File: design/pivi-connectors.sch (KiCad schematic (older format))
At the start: 13 parts, among them P1 Recom_Power_RAC10-05SC/277, P3 CONN_01X05, P4 CONN_01X02, P6 CONN_01X02, P7 CONN_01X05, P8 CONN_01X02, P9 CONN_02X20

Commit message: Fix #4: add GPIO to reset microcontroller from pi.
* Add a Raspeberry pi pin (GPIO 18) to reset microcontroller.
* Add a Raspebeery pi pin (GPIO 23) to control the microcontroller status.
* Add a RGB LED connected to the microcontroller (PD0, PD1, PD2).
* Rename all the sheets to PIVI v1.1.
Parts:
- C21: symbol C -> C-RESCUE-pivi-shield
- R9: symbol R -> R-RESCUE-pivi-shield
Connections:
- net labels added: GPIO-18, GPIO-23
- wire segments 48 -> 50
- no-connect marks 26 -> 24
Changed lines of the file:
@@
 EESchema Schematic File Version 2
+LIBS:pivi-shield-rescue
 LIBS:power
 LIBS:device
@@
 LIBS:memory
 LIBS:xilinx
-LIBS:special
 LIBS:microcontrollers
 LIBS:dsp
@@
 LIBS:txs0104e
 LIBS:less
+LIBS:pivi-shield-cache
 EELAYER 25 0
 EELAYER END
@@
 Sheet 3 12
 Title "PIVI"
-Date "sáb 01 nov 2014"
-Rev "1.0"
+Date "mar 23 jun 2015"
+Rev "1.1"
 Comp "Copyright (C) LESS industries S.A. 2014,2015"
 Comment1 "Share alike attribution non-commercial 4.0"
@@
 $EndDescr
 $Comp
-L +5V #PWR025
+L +5V #PWR026
 U 1 1 54959F0D
 P 7425 1625
-F 0 "#PWR025" H 7425 1715 20  0001 C CNN
+F 0 "#PWR026" H 7425 1715 20  0001 C CNN
 F 1 "+5V" H 7425 1750 30  0000 C CNN
 F 2 "" H 7425 1625 60  0000 C CNN
@@
 $EndComp
 $Comp
-L C C21
+L C-RESCUE-pivi-shield C21
 U 1 1 54959F13
 P 7425 1850
+AR Path="/54959F13" Ref="C21"  Part="1"
+AR Path="/549598FF/54959F13" Ref="C21"  Part="1"
 F 0 "C21" H 7425 1950 40  0000 L CNN
 F 1 "100nF" H 7431 1765 40  0000 L CNN
@@
 NoConn ~ 6550 2650
 NoConn ~ 6550 2450
-NoConn ~ 6550 2350
-NoConn ~ 6550 2150
 NoConn ~ 6550 3550
 NoConn ~ 6550 3450
@@
 Power line output.\nTo load.
 $Comp
-L +5V #PWR026
+L +5V #PWR027
 U 1 1 54959F4A
 P 3000 4675
-F 0 "#PWR026" H 3000 4765 20  0001 C CNN
+F 0 "#PWR027" H 3000 4765 20  0001 C CNN
 F 1 "+5V" H 3000 4800 30  0000 C CNN
 F 2 "" H 3000 4675 60  0000 C CNN
@@
 Power Line Connections
 $Comp
-L R R9
+L R-RESCUE-pivi-shield R9
 U 1 1 54959F58
 P 4425 4975
@@
 	1300 4575 1400 4575
 $Comp
-L GND #PWR027
+L GND-RESCUE-pivi-shield #PWR028
 U 1 1 54BFA08A
 P 7425 2075
-F 0 "#PWR027" H 7425 1825 60  0001 C CNN
+F 0 "#PWR028" H 7425 1825 60  0001 C CNN
 F 1 "GND" H 7425 1925 60  0000 C CNN
 F 2 "" H 7425 2075 60  0000 C CNN
@@
 $EndComp
 $Comp
-L GND #PWR028
+L GND-RESCUE-pivi-shield #PWR029
 U 1 1 54BFA09E
 P 6725 3300
-F 0 "#PWR028" H 6725 3050 60  0001 C CNN
+F 0 "#PWR029" H 6725 3050 60  0001 C CNN
 F 1 "GND" H 6725 3150 60  0000 C CNN
 F 2 "" H 6725 3300 60  0000 C CNN
@@
 $EndComp
 $Comp
-L GND #PWR029
+L GND-RESCUE-pivi-shield #PWR030
 U 1 1 54BFA0B2
 P 5900 3700
-F 0 "#PWR029" H 5900 3450 60  0001 C CNN
+F 0 "#PWR030" H 5900 3450 60  0001 C CNN
 F 1 "GND" H 5900 3550 60  0000 C CNN
 F 2 "" H 5900 3700 60  0000 C CNN
@@
 $EndComp
 $Comp
-L GND #PWR030
+L GND-RESCUE-pivi-shield #PWR031
 U 1 1 54BFA0C6
 P 4425 5275
-F 0 "#PWR030" H 4425 5025 60  0001 C CNN
+F 0 "#PWR031" H 4425 5025 60  0001 C CNN
 F 1 "GND" H 4425 5125 60  0000 C CNN
 F 2 "" H 4425 5275 60  0000 C CNN
@@
 $EndComp
 $Comp
-L GND #PWR031
+L GND-RESCUE-pivi-shield #PWR032
 U 1 1 54BFA203
 P 2625 4675
-F 0 "#PWR031" H 2625 4425 60  0001 C CNN
+F 0 "#PWR032" H 2625 4425 60  0001 C CNN
 F 1 "GND" H 2625 4525 60  0000 C CNN
 F 2 "" H 2625 4675 60  0000 C CNN
@@
 Alternative 5V power supply \nfor using when powering \nthe board externally.
 $Comp
-L GND #PWR032
+L GND-RESCUE-pivi-shield #PWR033
 U 1 1 54C181FB
 P 1350 5625
-F 0 "#PWR032" H 1350 5375 60  0001 C CNN
+F 0 "#PWR033" H 1350 5375 60  0001 C CNN
 F 1 "GND" H 1350 5475 60  0000 C CNN
 F 2 "" H 1350 5625 60  0000 C CNN
@@
 	1    0    0    -1
 $EndComp
+Wire Wire Line
+	6550 2150 6875 2150
+Text HLabel 6875 2150 2    60   Input ~ 0
+GPIO-18
+Wire Wire Line
+	6550 2350 6875 2350
+Text HLabel 6875 2350 2    60   Input ~ 0
+GPIO-23
 $EndSCHEMATC

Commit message: Fix #4: Move RGB LED from microcontroller to pi.
* Move RGB LED. Now it is controlled by the raspberry pi.
* Change some new libraries for capacitors and resistors.
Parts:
- added D2: LED_RGB, symbol LED_RGB
- added R1, R2, R3: 270, symbol R
- C21: symbol C-RESCUE-pivi-shield -> C
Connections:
- net labels added: GPIO-12, GPIO-24, GPIO-25
- wire segments 50 -> 64
- no-connect marks 24 -> 21
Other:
- note added: "The GPIO pins can draw 50mA safely, distributed\nacross all the pins; an individual GPIO pin can \nonly safely draw 16mA. \n\nhttps://www.raspberrypi.org/documentation/hardware/\nraspberrypi/power/README.md"
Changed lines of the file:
@@
 LIBS:txs0104e
 LIBS:less
-LIBS:pivi-shield-cache
 EELAYER 25 0
 EELAYER END
@@
 $EndDescr
 $Comp
-L +5V #PWR026
+L +5V #PWR025
 U 1 1 54959F0D
 P 7425 1625
-F 0 "#PWR026" H 7425 1715 20  0001 C CNN
+F 0 "#PWR025" H 7425 1715 20  0001 C CNN
 F 1 "+5V" H 7425 1750 30  0000 C CNN
 F 2 "" H 7425 1625 60  0000 C CNN
@@
 $EndComp
 $Comp
-L C-RESCUE-pivi-shield C21
+L C C21
 U 1 1 54959F13
 P 7425 1850
@@
 NoConn ~ 6550 2850
 NoConn ~ 6550 2750
-NoConn ~ 6550 2650
-NoConn ~ 6550 2450
 NoConn ~ 6550 3550
 NoConn ~ 6550 3450
 NoConn ~ 6550 3350
-NoConn ~ 6550 3150
 NoConn ~ 6050 3450
 NoConn ~ 6050 3350
@@
 Power line output.\nTo load.
 $Comp
-L +5V #PWR027
+L +5V #PWR026
 U 1 1 54959F4A
 P 3000 4675
-F 0 "#PWR027" H 3000 4765 20  0001 C CNN
+F 0 "#PWR026" H 3000 4765 20  0001 C CNN
 F 1 "+5V" H 3000 4800 30  0000 C CNN
 F 2 "" H 3000 4675 60  0000 C CNN
@@
 	6625 1750 6625 1650
 Wire Wire Line
-	7425 2050 7425 2075
-Wire Wire Line
-	7425 1650 7425 1625
+	7425 2000 7425 2075
+Wire Wire Line
+	7425 1625 7425 1700
 Wire Wire Line
 	6550 1850 6725 1850
@@
 	1300 4575 1400 4575
 $Comp
-L GND-RESCUE-pivi-shield #PWR028
+L GND-RESCUE-pivi-shield #PWR027
 U 1 1 54BFA08A
 P 7425 2075
-F 0 "#PWR028" H 7425 1825 60  0001 C CNN
+F 0 "#PWR027" H 7425 1825 60  0001 C CNN
 F 1 "GND" H 7425 1925 60  0000 C CNN
 F 2 "" H 7425 2075 60  0000 C CNN
@@
 $EndComp
 $Comp
-L GND-RESCUE-pivi-shield #PWR029
+L GND-RESCUE-pivi-shield #PWR028
 U 1 1 54BFA09E
 P 6725 3300
-F 0 "#PWR029" H 6725 3050 60  0001 C CNN
+F 0 "#PWR028" H 6725 3050 60  0001 C CNN
 F 1 "GND" H 6725 3150 60  0000 C CNN
 F 2 "" H 6725 3300 60  0000 C CNN
@@
 $EndComp
 $Comp
-L GND-RESCUE-pivi-shield #PWR030
+L GND-RESCUE-pivi-shield #PWR029
 U 1 1 54BFA0B2
 P 5900 3700
-F 0 "#PWR030" H 5900 3450 60  0001 C CNN
+F 0 "#PWR029" H 5900 3450 60  0001 C CNN
 F 1 "GND" H 5900 3550 60  0000 C CNN
 F 2 "" H 5900 3700 60  0000 C CNN
@@
 $EndComp
 $Comp
-L GND-RESCUE-pivi-shield #PWR031
+L GND-RESCUE-pivi-shield #PWR030
 U 1 1 54BFA0C6
 P 4425 5275
-F 0 "#PWR031" H 4425 5025 60  0001 C CNN
+F 0 "#PWR030" H 4425 5025 60  0001 C CNN
 F 1 "GND" H 4425 5125 60  0000 C CNN
 F 2 "" H 4425 5275 60  0000 C CNN
@@
 $EndComp
 $Comp
-L GND-RESCUE-pivi-shield #PWR032
+L GND-RESCUE-pivi-shield #PWR031
 U 1 1 54BFA203
 P 2625 4675
-F 0 "#PWR032" H 2625 4425 60  0001 C CNN
+F 0 "#PWR031" H 2625 4425 60  0001 C CNN
 F 1 "GND" H 2625 4525 60  0000 C CNN
 F 2 "" H 2625 4675 60  0000 C CNN
@@
 Alternative 5V power supply \nfor using when powering \nthe board externally.
 $Comp
-L GND-RESCUE-pivi-shield #PWR033
+L GND-RESCUE-pivi-shield #PWR032
 U 1 1 54C181FB
 P 1350 5625
-F 0 "#PWR033" H 1350 5375 60  0001 C CNN
+F 0 "#PWR032" H 1350 5375 60  0001 C CNN
 F 1 "GND" H 1350 5475 60  0000 C CNN
 F 2 "" H 1350 5625 60  0000 C CNN
@@
 Text HLabel 6875 2350 2    60   Input ~ 0
 GPIO-23
+Connection ~ 7425 1650
+$Comp
+L LED_RGB D2
+U 1 1 558C1006
+P 7600 2950
+F 0 "D2" H 7600 3400 50  0000 C CNN
+F 1 "LED_RGB" H 7600 3300 50  0000 C CNN
+F 2 "" H 7600 2900 60  0000 C CNN
+F 3 "" H 7600 2900 60  0000 C CNN
+	1    7600 2950
+	-1   0    0    1
+$EndComp
+$Comp
+L R R1
+U 1 1 558C1041
+P 8175 2750
+F 0 "R1" V 8255 2750 50  0000 C CNN
+F 1 "270" V 8175 2750 50  0000 C CNN
+F 2 "" V 8105 2750 30  0000 C CNN
+F 3 "" H 8175 2750 30  0000 C CNN
+	1    8175 2750
+	0    -1   -1   0
+$EndComp
+$Comp
+L R R2
+U 1 1 558C1113
+P 8175 2950
+F 0 "R2" V 8255 2950 50  0000 C CNN
+F 1 "270" V 8175 2950 50  0000 C CNN
+F 2 "" V 8105 2950 30  0000 C CNN
+F 3 "" H 8175 2950 30  0000 C CNN
+	1    8175 2950
+	0    -1   -1   0
+$EndComp
+$Comp
+L R R3
+U 1 1 558C1151
+P 8175 3150
+F 0 "R3" V 8255 3150 50  0000 C CNN
+F 1 "270" V 8175 3150 50  0000 C CNN
+F 2 "" V 8105 3150 30  0000 C CNN
+F 3 "" H 8175 3150 30  0000 C CNN
+	1    8175 3150
+	0    -1   -1   0
+$EndComp
+Wire Wire Line
+	7900 2750 8025 2750
+Wire Wire Line
+	7900 2950 8025 2950
+Wire Wire Line
+	7900 3150 8025 3150
+Wire Wire Line
+	8325 2750 8550 2750
+Wire Wire Line
+	8550 2750 8550 3350
+Wire Wire Line
+	8325 3150 8550 3150
+Connection ~ 8550 3150
+Wire Wire Line
+	8325 2950 8550 2950
+Connection ~ 8550 2950
+Text Label 6875 2750 0    60   ~ 0
+GPIO-24
+Wire Wire Line
+	6550 2650 6800 2650
+Wire Wire Line
+	6800 2650 6800 2950
+Text Label 6875 2950 0    60   ~ 0
+GPIO-25
+Wire Wire Line
+	6875 2450 6875 2750
+Wire Wire Line
+	6875 2450 6550 2450
+Wire Wire Line
+	6550 3150 7300 3150
+Text Label 6875 3150 0    60   ~ 0
+GPIO-12
+$Comp
+L GND #PWR033
+U 1 1 558C16FC
+P 8550 3350
+F 0 "#PWR033" H 8550 3100 50  0001 C CNN
+F 1 "GND" H 8550 3200 50  0000 C CNN
+F 2 "" H 8550 3350 60  0000 C CNN
+F 3 "" H 8550 3350 60  0000 C CNN
+	1    8550 3350
+	1    0    0    -1
+$EndComp
+Text Notes 8650 3200 0    60   ~ 0
+The GPIO pins can draw 50mA safely, distributed\nacross all the pins; an individual GPIO pin can \nonly safely draw 16mA. \n\nhttps://www.raspberrypi.org/documentation/hardware/\nraspberrypi/power/README.md
+Wire Wire Line
+	6800 2950 7300 2950
+Wire Wire Line
+	6875 2750 7300 2750
 $EndSCHEMATC

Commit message: Changing footprints of  audio jack3.5mm Added new footprints. Added debub uart,  reference voltage Added two extra circuits for voltage measure Moving to PIVI 2.0, added circuits for current clamps
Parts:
- removed P3, P7: CONN_01X05, LESS:CONN-TERM-BLK-5POS-PHOENIX, symbol CONN_01X05
- removed P8: CONN_01X02, LESS:CONN-TERM-BLK-2POS-PHOENIX, symbol CONN_01X02
- removed R1, R2, R3: 270, symbol R
- added P6: CONN_01X04, symbol CONN_01X04
- added R7, R8, R9: 270, Resistors_SMD:R_0603, symbol R
- D2: footprint (none) -> LEDs:LED_RGB_PLLC-6
- R6: renamed from R9; symbol R-RESCUE-pivi-shield -> R
- renumbered C21 to C11, L15 to L4, L16 to L5, P6 to P2, P1 to P3, P9 to P5
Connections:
- net labels added: +3.3VP, CT1_1, CT1_2, CT1_DETECTOR, CT2_1, CT2_2, CT2_DETECTOR, CT3_1, CT3_2, CT3_DETECTOR, CT4_1, CT4_2, CT4_DETECTOR, CT5_1, CT5_2, CT5_DETECTOR, CT6_1, CT6_2, CT6_DETECTOR, Neutral_Line, Phase_Line
- net labels removed: Neutral1_In, Neutral1_Out, Phase1_In, Phase1_Out, Phase2_In, Phase2_Out, Phase3_In, Phase3_Out, Phase4_In, Phase4_Out, Phase5_In, Phase5_Out, Phase6_In, Phase6_Out
- wire segments 64 -> 78
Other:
- note added: "Audio Jack 3.5 mm female connector\n"
- note added: "Clamp audio connections for SCT-013-000"
- note added: "Debug Uart"
- note added: "SJ-3506-SMT"
- note added: "The GPIO pins can draw 50mA safely, distributed\nacross all the pins; an individual GPIO pin can \nonly safely draw 16mA. \n\nhttps://www.raspberrypi.org/documentation/hardw"
- note added: "This connector must meet the following requirements:\n* Internal switch : Avoids noise in pins when the clamp is unplugged.\n* Shielded : Increase endurance, stregth and avoid noise."
- note removed: "277-9761-ND"
- note removed: "Power line output.\nTo load."
- note removed: "The GPIO pins can draw 50mA safely, distributed\nacross all the pins; an individual GPIO pin can \nonly safely draw 16mA. \n\nhttps://www.raspberrypi.org/documentation/hardware/\nraspberrypi/power/README.md"
- moved on the sheet: C11, D1, JP1, L4, L5, P2, P3, P4, P5

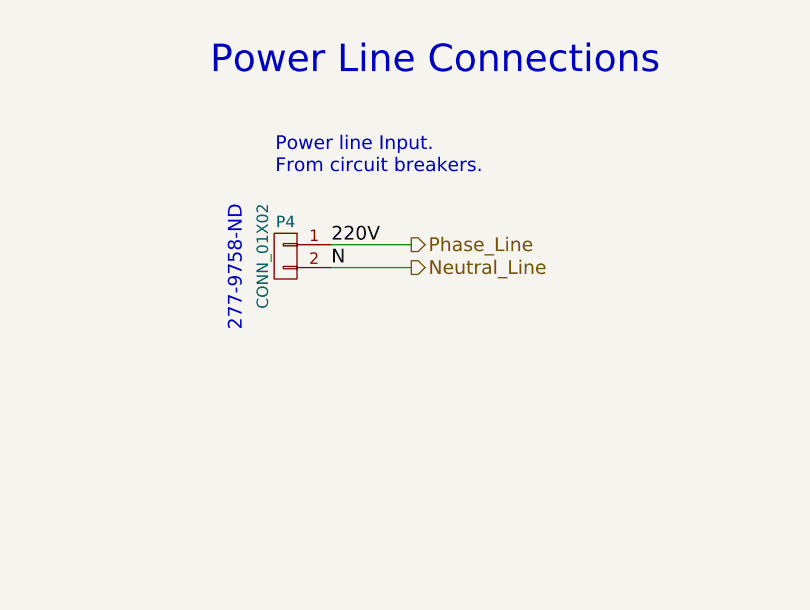
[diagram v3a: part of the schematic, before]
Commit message: Fix connection problems.
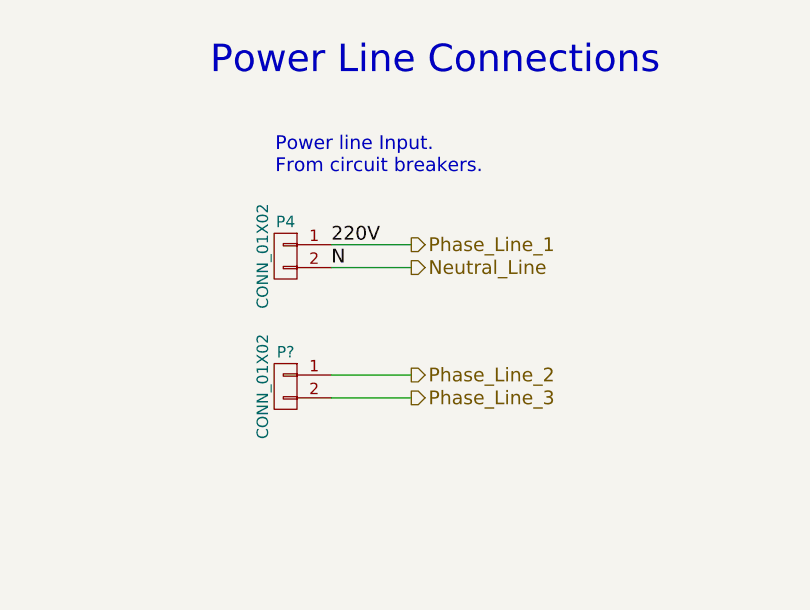
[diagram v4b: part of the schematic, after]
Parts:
- added P?: CONN_01X02, LESS:CONN-TERM-BLK-2POS-PHOENIX, symbol CONN_01X02
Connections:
- net Phase_Line renamed Phase_Line_1
- new net Phase_Line_2: P?.1 (P1)
- new net Phase_Line_3: P?.2 (P2)
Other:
- note removed: "277-9758-ND"
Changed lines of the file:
@@
 Board power Supply Connections
 Text HLabel 6610 5160 2    60   Output ~ 0
-Phase_Line
+Phase_Line_1
 Text HLabel 6610 5260 2    60   Output ~ 0
 Neutral_Line
@@
 F4 "CT_DETECTOR" I L 1450 2000 60
 $EndSheet
-Text Notes 5875 5540 1    60   ~ 0
-277-9758-ND
 Text HLabel 1300 2000 0    60   Input ~ 0
 CT1_DETECTOR
@@
 Wire Wire Line
 	9070 5205 9240 5205
+Text HLabel 6610 5730 2    60   Output ~ 0
+Phase_Line_2
+Text HLabel 6610 5830 2    60   Output ~ 0
+Phase_Line_3
+$Comp
+L CONN_01X02 P?
+U 1 1 55BC87D7
+P 6060 5780
+F 0 "P?" H 6060 5930 50  0000 C CNN
+F 1 "CONN_01X02" V 6160 5780 50  0000 C CNN
+F 2 "LESS:CONN-TERM-BLK-2POS-PHOENIX" H 6060 5780 60  0001 C CNN
+F 3 "" H 6060 5780 60  0000 C CNN
+	1    6060 5780
+	-1   0    0    -1
+$EndComp
+Wire Wire Line
+	6260 5830 6610 5830
+Wire Wire Line
+	6260 5730 6610 5730
 $EndSCHEMATC

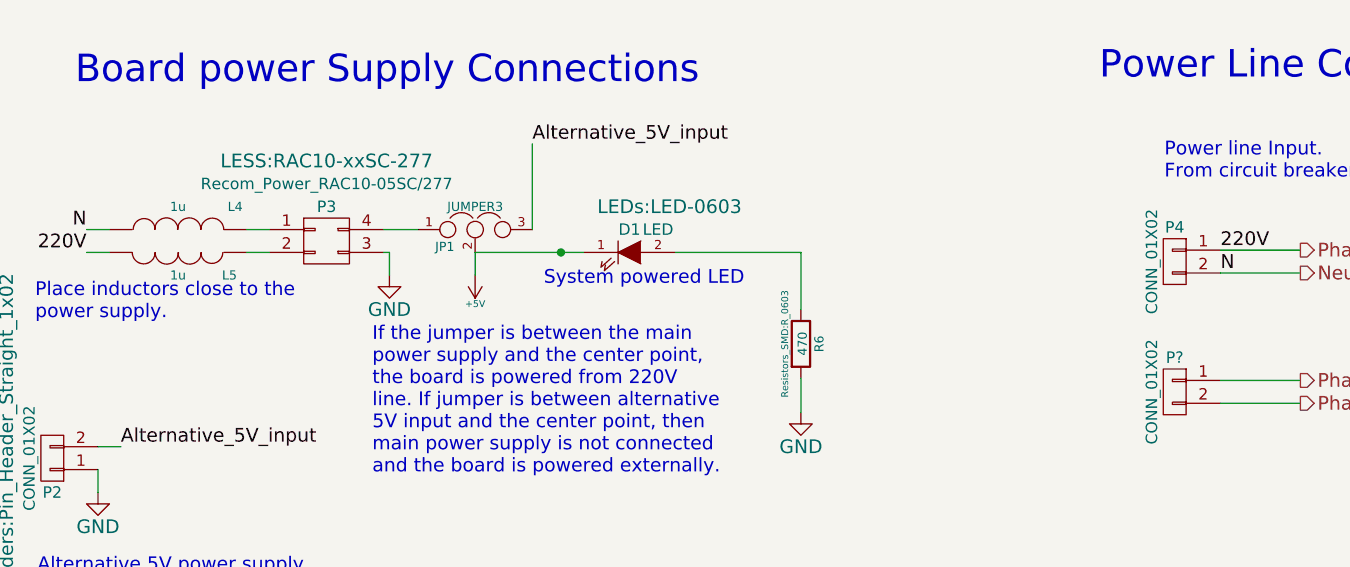
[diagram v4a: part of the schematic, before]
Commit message: Starting PIVI 2.0 * sch ready. * components in PCB placed.
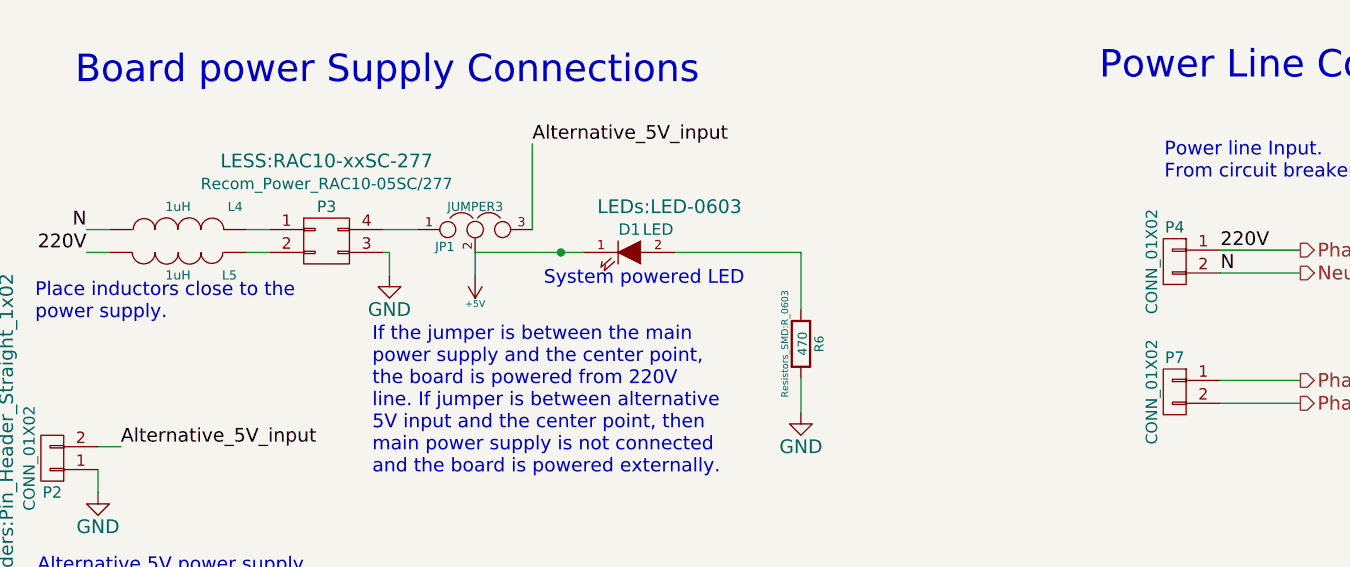
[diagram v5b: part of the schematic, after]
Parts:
- L4, L5: value 1u -> 1uH
- P4: footprint LESS:CONN-TERM-BLK-2POS-PHOENIX -> Connect:bornier2
- P6: footprint (none) -> Pin_Headers:Pin_Header_Straight_1x04
- P7: renamed from P?; footprint LESS:CONN-TERM-BLK-2POS-PHOENIX -> Connect:bornier2
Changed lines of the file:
@@
 $EndDescr
 $Comp
-L +5V #PWR27
+L +5V #PWR026
 U 1 1 54959F0D
 P 8390 1240
-F 0 "#PWR27" H 8390 1330 20  0001 C CNN
+F 0 "#PWR026" H 8390 1330 20  0001 C CNN
 F 1 "+5V" H 8390 1365 30  0000 C CNN
 F 2 "" H 8390 1240 60  0000 C CNN
@@
 Power line Input.\nFrom circuit breakers.
 $Comp
-L +5V #PWR23
+L +5V #PWR027
 U 1 1 54959F4A
 P 3000 5270
-F 0 "#PWR23" H 3000 5360 20  0001 C CNN
+F 0 "#PWR027" H 3000 5360 20  0001 C CNN
 F 1 "+5V" H 3000 5395 30  0000 C CNN
 F 2 "" H 3000 5270 60  0000 C CNN
@@
 P 1700 5070
 F 0 "L4" V 1800 4820 40  0000 C CNN
-F 1 "1u" V 1800 5070 40  0000 C CNN
+F 1 "1uH" V 1800 5070 40  0000 C CNN
 F 2 "SMD_Packages:SMD-0603" H 1700 5070 60  0001 C CNN
 F 3 "" H 1700 5070 60  0000 C CNN
@@
 P 1700 5170
 F 0 "L5" V 1800 5395 40  0000 C CNN
-F 1 "1u" V 1800 5170 40  0000 C CNN
+F 1 "1uH" V 1800 5170 40  0000 C CNN
 F 2 "SMD_Packages:SMD-0603" H 1700 5170 60  0001 C CNN
 F 3 "" H 1700 5170 60  0000 C CNN
@@
 $EndComp
 $Comp
-L GND #PWR28
+L GND #PWR028
 U 1 1 54BFA08A
 P 8390 1690
-F 0 "#PWR28" H 8390 1440 60  0001 C CNN
+F 0 "#PWR028" H 8390 1440 60  0001 C CNN
 F 1 "GND" H 8390 1540 60  0000 C CNN
 F 2 "" H 8390 1690 60  0000 C CNN
@@
 $EndComp
 $Comp
-L GND #PWR26
+L GND #PWR029
 U 1 1 54BFA09E
 P 7690 2915
-F 0 "#PWR26" H 7690 2665 60  0001 C CNN
+F 0 "#PWR029" H 7690 2665 60  0001 C CNN
 F 1 "GND" H 7690 2765 60  0000 C CNN
 F 2 "" H 7690 2915 60  0000 C CNN
@@
 $EndComp
 $Comp
-L GND #PWR25
+L GND #PWR030
 U 1 1 54BFA0B2
 P 6865 3315
-F 0 "#PWR25" H 6865 3065 60  0001 C CNN
+F 0 "#PWR030" H 6865 3065 60  0001 C CNN
 F 1 "GND" H 6865 3165 60  0000 C CNN
 F 2 "" H 6865 3315 60  0000 C CNN
@@
 $EndComp
 $Comp
-L GND #PWR24
+L GND #PWR031
 U 1 1 54BFA0C6
 P 4425 5870
-F 0 "#PWR24" H 4425 5620 60  0001 C CNN
+F 0 "#PWR031" H 4425 5620 60  0001 C CNN
 F 1 "GND" H 4425 5720 60  0000 C CNN
 F 2 "" H 4425 5870 60  0000 C CNN
@@
 $EndComp
 $Comp
-L GND #PWR22
+L GND #PWR032
 U 1 1 54BFA203
 P 2625 5270
-F 0 "#PWR22" H 2625 5020 60  0001 C CNN
+F 0 "#PWR032" H 2625 5020 60  0001 C CNN
 F 1 "GND" H 2625 5120 60  0000 C CNN
 F 2 "" H 2625 5270 60  0000 C CNN
@@
 Alternative 5V power supply \nfor using when powering \nthe board externally.
 $Comp
-L GND #PWR21
+L GND #PWR033
 U 1 1 54C181FB
 P 1350 6220
-F 0 "#PWR21" H 1350 5970 60  0001 C CNN
+F 0 "#PWR033" H 1350 5970 60  0001 C CNN
 F 1 "GND" H 1350 6070 60  0000 C CNN
 F 2 "" H 1350 6220 60  0000 C CNN
@@
 F 0 "P4" H 6060 5360 50  0000 C CNN
 F 1 "CONN_01X02" V 6160 5210 50  0000 C CNN
-F 2 "LESS:CONN-TERM-BLK-2POS-PHOENIX" H 6060 5210 60  0001 C CNN
+F 2 "Connect:bornier2" H 6060 5210 60  0001 C CNN
 F 3 "" H 6060 5210 60  0000 C CNN
 	1    6060 5210
@@
 	9440 2190 9440 2915
 $Comp
-L GND #PWR31
+L GND #PWR034
 U 1 1 55BA8447
 P 9440 2915
-F 0 "#PWR31" H 9440 2665 60  0001 C CNN
+F 0 "#PWR034" H 9440 2665 60  0001 C CNN
 F 1 "GND" H 9440 2765 60  0000 C CNN
 F 2 "" H 9440 2915 60  0000 C CNN
@@
 F 0 "P6" H 8870 5405 50  0000 C CNN
 F 1 "CONN_01X04" V 8970 5155 50  0000 C CNN
-F 2 "" H 8870 5155 60  0000 C CNN
+F 2 "Pin_Headers:Pin_Header_Straight_1x04" H 8870 5155 60  0001 C CNN
 F 3 "" H 8870 5155 60  0000 C CNN
 	1    8870 5155
@@
 $EndComp
 $Comp
-L +3.3VP #PWR29
+L +3.3VP #PWR035
 U 1 1 55BEAB18
 P 9330 4940
-F 0 "#PWR29" H 9480 4890 50  0001 C CNN
+F 0 "#PWR035" H 9480 4890 50  0001 C CNN
 F 1 "+3.3VP" H 9330 5040 50  0000 C CNN
 F 2 "" H 9330 4940 60  0000 C CNN
@@
 	9335 5305 9335 5365
 $Comp
-L GND #PWR30
+L GND #PWR036
 U 1 1 55BEFFD5
 P 9335 5365
-F 0 "#PWR30" H 9335 5115 50  0001 C CNN
+F 0 "#PWR036" H 9335 5115 50  0001 C CNN
 F 1 "GND" H 9335 5215 50  0000 C CNN
 F 2 "" H 9335 5365 60  0000 C CNN
@@
 Phase_Line_3
 $Comp
-L CONN_01X02 P?
+L CONN_01X02 P7
 U 1 1 55BC87D7
 P 6060 5780
-F 0 "P?" H 6060 5930 50  0000 C CNN
+F 0 "P7" H 6060 5930 50  0000 C CNN
 F 1 "CONN_01X02" V 6160 5780 50  0000 C CNN
-F 2 "LESS:CONN-TERM-BLK-2POS-PHOENIX" H 6060 5780 60  0001 C CNN
+F 2 "Connect:bornier2" H 6060 5780 60  0001 C CNN
 F 3 "" H 6060 5780 60  0000 C CNN
 	1    6060 5780

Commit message: PCB routed + BOM complete
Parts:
- L4, L5: footprint SMD_Packages:SMD-0603 -> Resistors_SMD:R_0603
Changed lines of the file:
@@
 F 0 "L4" V 1800 4820 40  0000 C CNN
 F 1 "1uH" V 1800 5070 40  0000 C CNN
-F 2 "SMD_Packages:SMD-0603" H 1700 5070 60  0001 C CNN
+F 2 "Resistors_SMD:R_0603" H 1700 5070 60  0001 C CNN
 F 3 "" H 1700 5070 60  0000 C CNN
 	1    1700 5070
@@
 F 0 "L5" V 1800 5395 40  0000 C CNN
 F 1 "1uH" V 1800 5170 40  0000 C CNN
-F 2 "SMD_Packages:SMD-0603" H 1700 5170 60  0001 C CNN
+F 2 "Resistors_SMD:R_0603" H 1700 5170 60  0001 C CNN
 F 3 "" H 1700 5170 60  0000 C CNN
 	1    1700 5170
